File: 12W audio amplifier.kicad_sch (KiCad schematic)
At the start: 19 parts

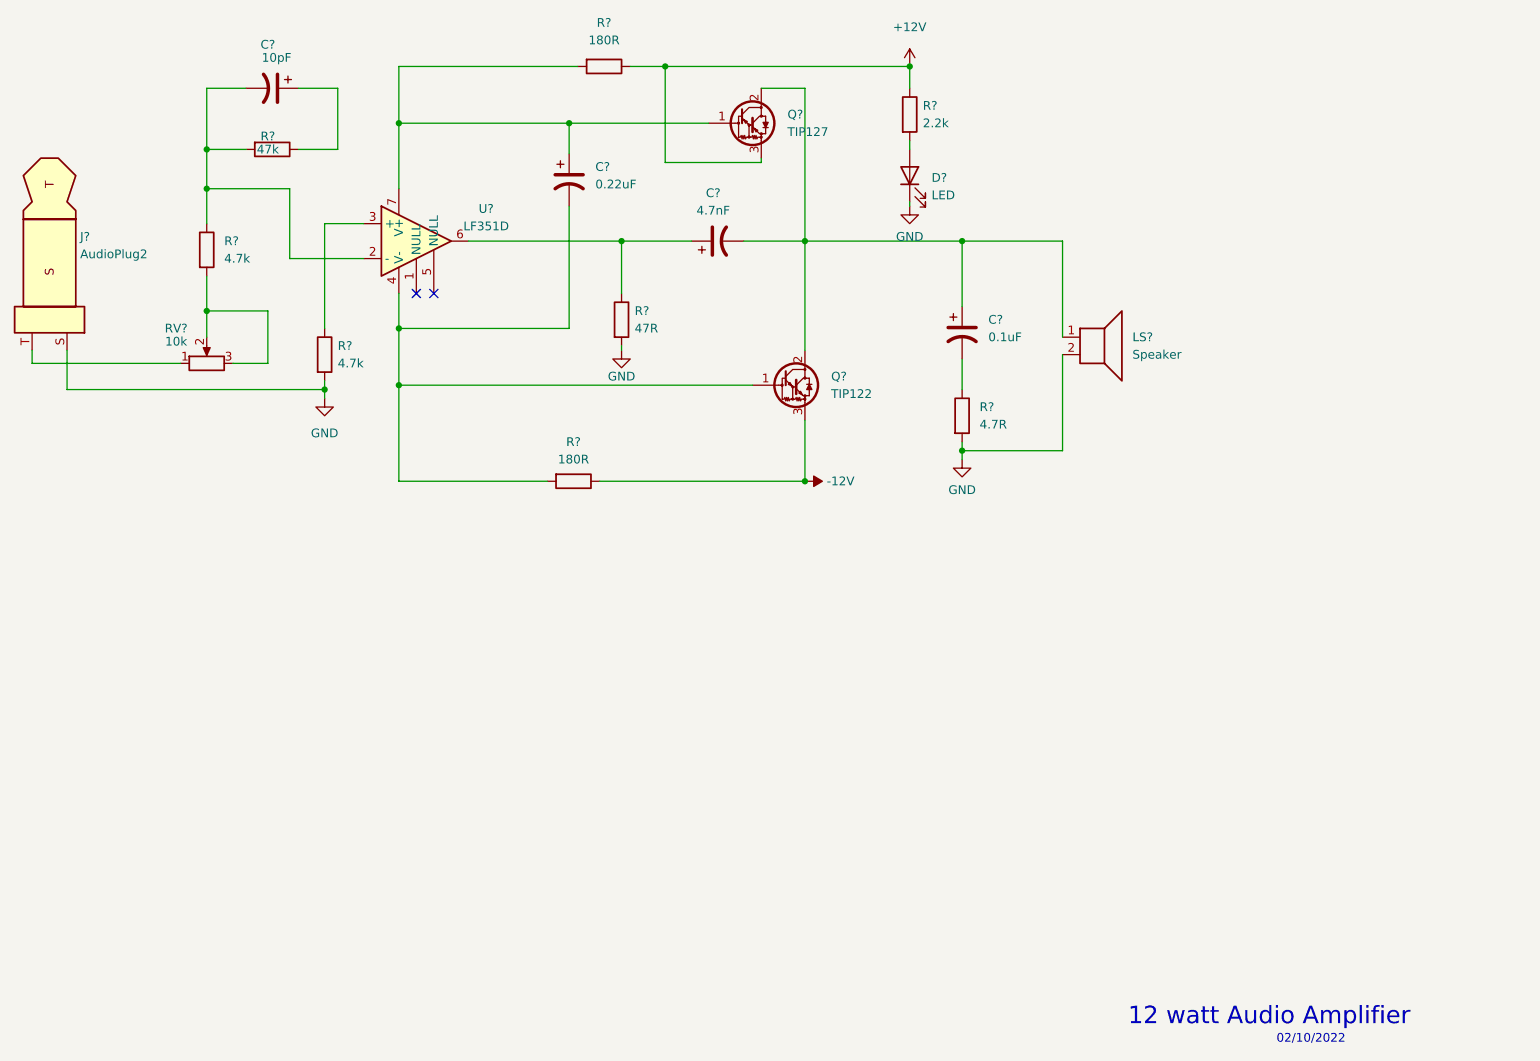
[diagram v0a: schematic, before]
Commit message: updated schematic diagram
annotations,footprints setup
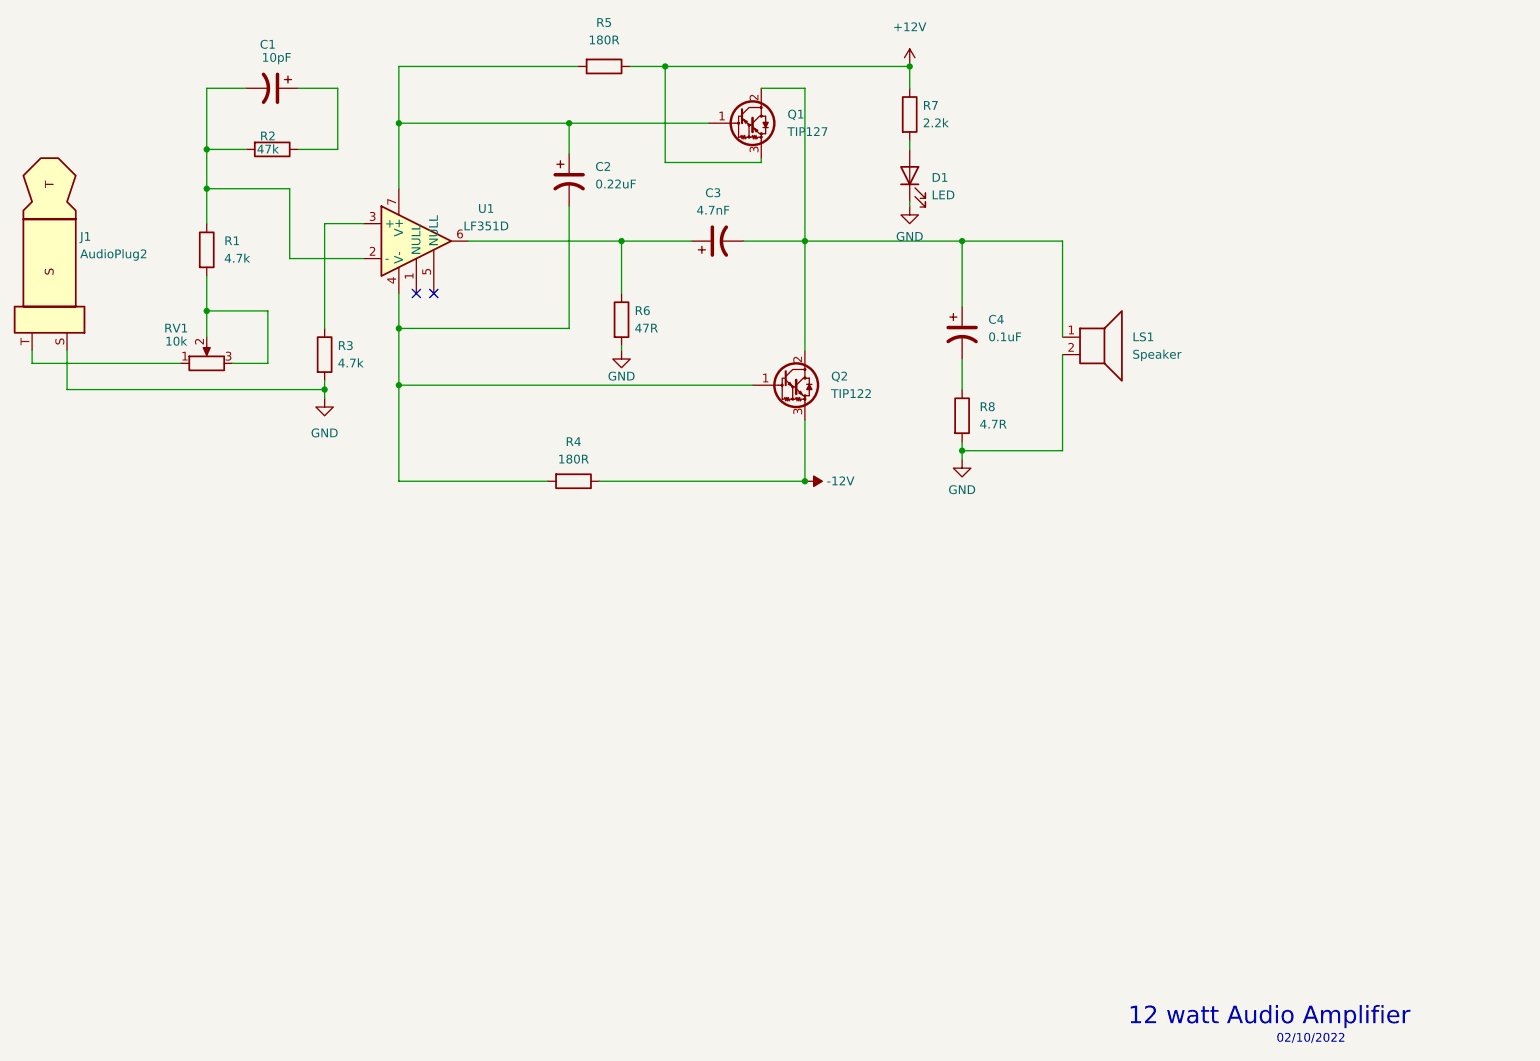
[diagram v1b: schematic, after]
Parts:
- LS1: renamed from LS?; footprint (none) -> Connector_PinHeader_1.27mm:PinHeader_1x02_P1.27mm_Vertical
- gave numbers to parts that had none: 18
